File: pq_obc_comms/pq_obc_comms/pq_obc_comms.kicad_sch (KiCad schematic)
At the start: 70 parts, among them J1 Conn_01x10, J2 Conn_01x10, J3 Conn_01x10, J4 Conn_01x10, J6 U.FL, U1 STM32L476RGTx, U2 SX1262IMLTRT, U3 BD2232G-GTR, U4 BD2232G-GTR, U5 BGS12PL6E6327XTSA1, U6 BD2232G-GTR, U7 BD2232G-GTR, X1 ECS-120-18-33-JEM-TR3, X2 FA-128_32.0000MF20X-K5, X3 ABS09-32.768KHZ-7-T

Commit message: Functional revision and finishing touches part II
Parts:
- added Annotation1: Silkscreen_Annotation, symbols-nsl:Bike, symbol symbols-nsl:Silkscreen_Annotation
- U5: footprint GGS_RF:PG-TSLP-6-4 -> rf-nsl:PG-TSLP-6-4
- X1: footprint GGS_Miscellaneous:ECX-32 -> miscelaneous-nsl:ECX-32
- X2: footprint GGS_Miscellaneous:EPSON_FA128 -> miscelaneous-nsl:EPSON_FA128
- X3: footprint GGS_Miscellaneous:ABS09 -> miscelaneous-nsl:ABS09
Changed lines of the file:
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@@
     (pin "1")
   )
+  (symbol (lib_id "symbols-nsl:Silkscreen_Annotation") (at 247.65 58.42 0) (unit 1)
+    (in_bom yes) (on_board yes) (fields_autoplaced)
+    (property "Reference" "Annotation1" (id 0) (at 254 51.4349 0)
+      (effects (font (size 1.27 1.27)) (justify left))
+    )
+    (property "Value" "Silkscreen_Annotation" (id 1) (at 254 53.9749 0)
+      (effects (font (size 1.27 1.27)) (justify left))
+    )
+    (property "Footprint" "symbols-nsl:Bike" (id 2) (at 247.65 58.42 0)
+      (effects (font (size 1.27 1.27)) hide)
+    )
+    (property "Datasheet" "" (id 3) (at 247.65 58.42 0)
+      (effects (font (size 1.27 1.27)) hide)
+    )
+  )
   (symbol (lib_id "power:GND") (at 116.84 25.4 0) (unit 1)
     (in_bom yes) (on_board yes)
@@
     (property "Reference" "U5" (id 0) (at 184.15 22.86 0))
     (property "Value" "BGS12PL6E6327XTSA1" (id 1) (at 184.15 25.4 0))
-    (property "Footprint" "GGS_RF:PG-TSLP-6-4" (id 2) (at 184.15 33.02 0)
+    (property "Footprint" "rf-nsl:PG-TSLP-6-4" (id 2) (at 184.15 33.02 0)
       (effects (font (size 1.27 1.27)) hide)
     )
@@
       (effects (font (size 1.27 1.27)) (justify left))
     )
-    (property "Footprint" "GGS_Miscellaneous:EPSON_FA128" (id 2) (at 259.08 29.21 0)
+    (property "Footprint" "miscelaneous-nsl:EPSON_FA128" (id 2) (at 259.08 29.21 0)
       (effects (font (size 1.27 1.27)) hide)
     )
@@
     (property "Reference" "X3" (id 0) (at 219.71 142.24 0))
     (property "Value" "ABS09-32.768KHZ-7-T" (id 1) (at 219.71 144.78 0))
-    (property "Footprint" "GGS_Miscellaneous:ABS09" (id 2) (at 219.71 148.59 0)
+    (property "Footprint" "miscelaneous-nsl:ABS09" (id 2) (at 219.71 148.59 0)
       (effects (font (size 1.27 1.27)) hide)
     )
@@
       (effects (font (size 1.27 1.27)) (justify left))
     )
-    (property "Footprint" "GGS_Miscellaneous:ECX-32" (id 2) (at 260.35 151.13 0)
+    (property "Footprint" "miscelaneous-nsl:ECX-32" (id 2) (at 260.35 151.13 0)
       (effects (font (size 1.27 1.27)) hide)
     )
@@
       (reference "#PWR0149") (unit 1) (value "GND") (footprint "")
     )
+    (path "/0e0a9cdf-3063-4090-b911-679c5a730d38"
+      (reference "Annotation1") (unit 1) (value "Silkscreen_Annotation") (footprint "symbols-nsl:Bike")
+    )
     (path "/70f6326e-6380-4875-aac5-5e40eda2ece8"
       (reference "C1") (unit 1) (value "47nF") (footprint "Capacitor_SMD:C_0402_1005Metric")
@@
     )
     (path "/1e73ef1c-3a42-4d69-9bb9-affa28519ebc"
-      (reference "U5") (unit 1) (value "BGS12PL6E6327XTSA1") (footprint "GGS_RF:PG-TSLP-6-4")
+      (reference "U5") (unit 1) (value "BGS12PL6E6327XTSA1") (footprint "rf-nsl:PG-TSLP-6-4")
     )
     (path "/5b2c5bc3-5fa8-4d93-ab7a-d6c8c3adc44e"
@@
     )
     (path "/aee54727-eead-440f-9fa9-5ccf5d66a20e"
-      (reference "X1") (unit 1) (value "ECS-120-18-33-JEM-TR3") (footprint "GGS_Miscellaneous:ECX-32")
+      (reference "X1") (unit 1) (value "ECS-120-18-33-JEM-TR3") (footprint "miscelaneous-nsl:ECX-32")
     )
     (path "/7ef30fbc-71e7-4186-a1d8-48087b5069c5"
-      (reference "X2") (unit 1) (value "FA-128_32.0000MF20X-K5") (footprint "GGS_Miscellaneous:EPSON_FA128")
+      (reference "X2") (unit 1) (value "FA-128_32.0000MF20X-K5") (footprint "miscelaneous-nsl:EPSON_FA128")
     )
     (path "/89691019-6129-4efd-9407-b4187a9c6ccc"
-      (reference "X3") (unit 1) (value "ABS09-32.768KHZ-7-T") (footprint "GGS_Miscellaneous:ABS09")
+      (reference "X3") (unit 1) (value "ABS09-32.768KHZ-7-T") (footprint "miscelaneous-nsl:ABS09")
     )
   )

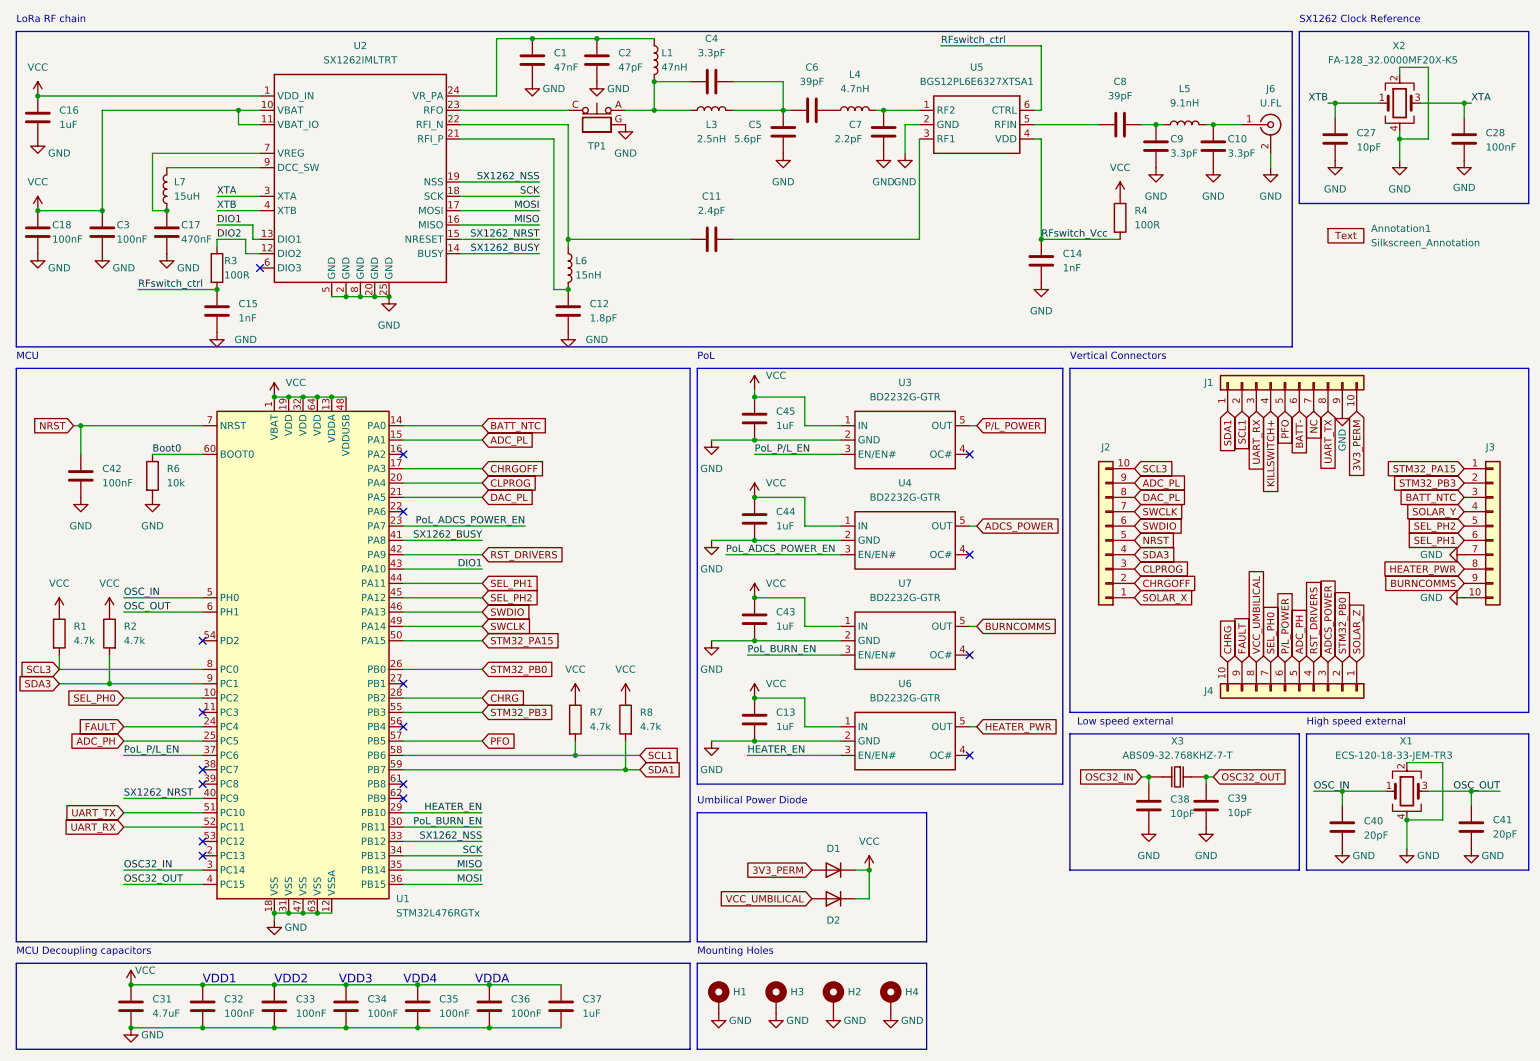
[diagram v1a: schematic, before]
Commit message: Full Kicad7 transition, library improvement and adaptation, correct footprints and 3D models added
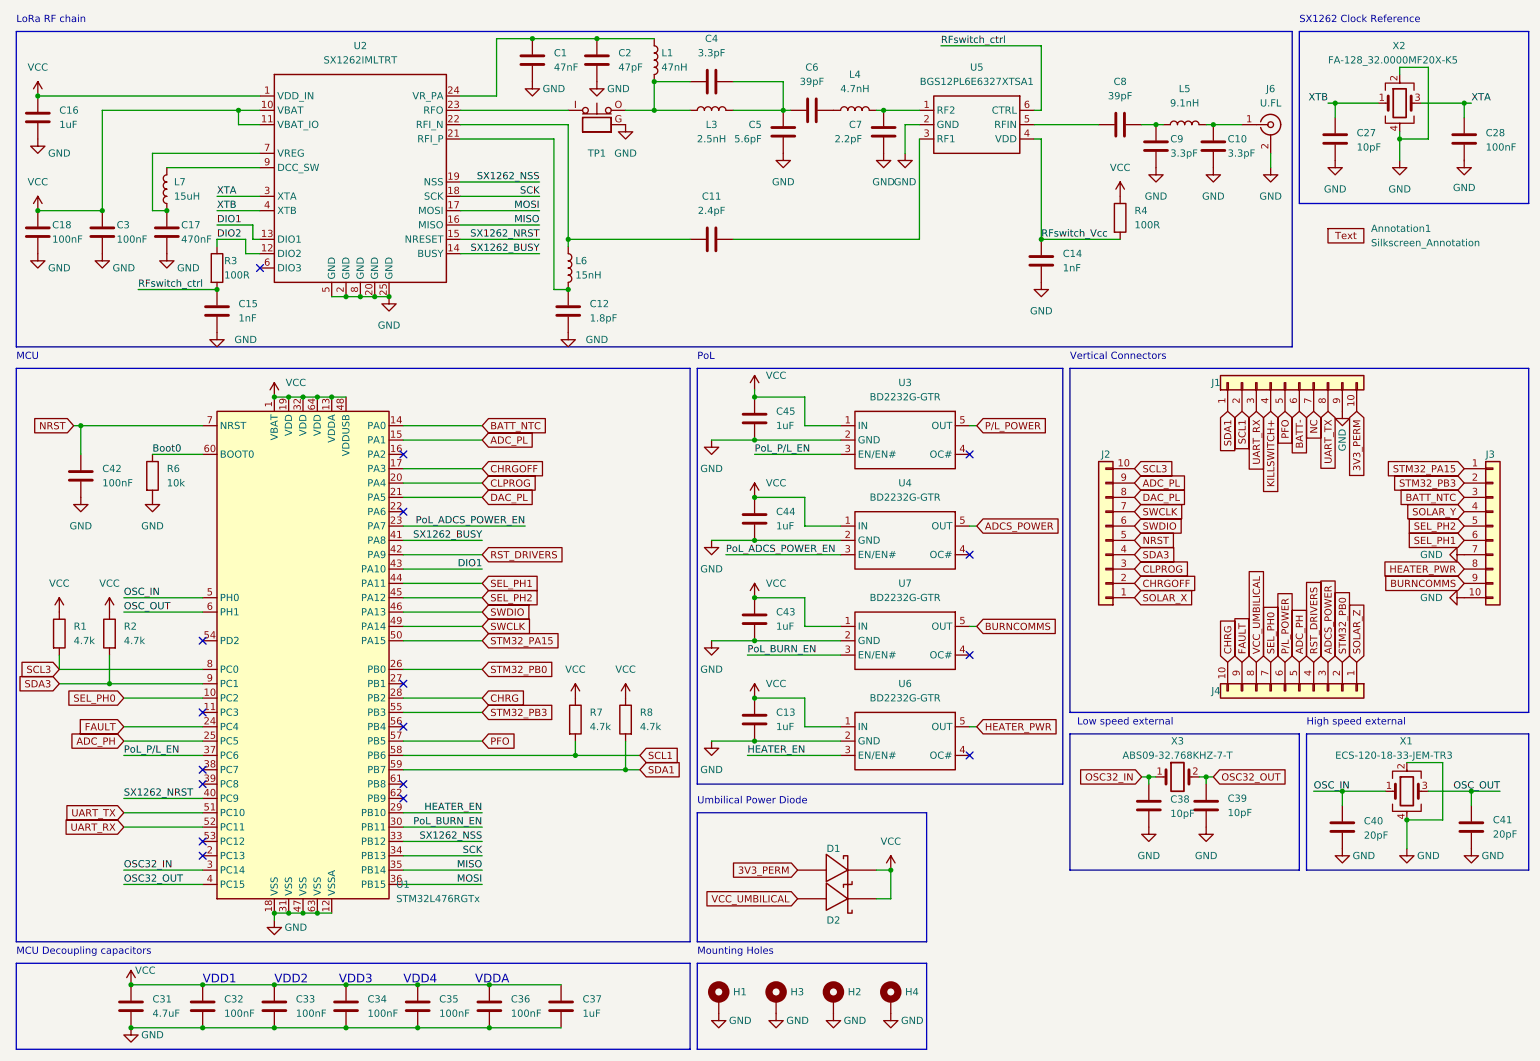
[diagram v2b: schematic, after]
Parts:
- Annotation1: footprint symbols-nsl:Bike -> -nsl_symbols:Bike; symbol symbols-nsl:Silkscreen_Annotation -> -nsl_symbols:Silkscreen_Annotation
- D1, D2: value RBS1LAM40ATR -> ${SIM.PARAMS}; footprint Diode_SMD:D_SOD-128 -> -nsl_passive:RBS1LAM40ATR_Schottky; symbol Simulation_SPICE:DIODE -> -nsl_passive:RBS1LAM40ATR_Schottky; Spice_Netlist_Enabled Y -> (none); Spice_Primitive D -> (none)
- J1, J2, J3, J4: footprint Connector_PinSocket_2.54mm:PinSocket_1x10_P2.54mm_Vertical -> -nsl_connector:SLW-110-01; symbol Connector_Generic:Conn_01x10 -> -nsl_connector:SLW-110-01
- TP1: footprint Connector_Coaxial:CoaxialSwitch_Hirose_MS-156C3_Horizontal -> -nsl_connector:CoaxialSwitch_Hirose_MS-156C3_Horizontal; symbol Connector:CoaxialSwitch_Testpoint -> -nsl_connector:MS-156C
- U1: symbol MCU_ST_STM32L4:STM32L476RGTx -> -nsl_mcu:STM32L476RGT
- U2: symbol COMMS-altium-import:0_SX1262IMLTRT -> -nsl_rf:SX1262IML
- U3, U4, U6, U7: symbol COMMS-altium-import:0_BD2232G-GTR -> -nsl_power:BD2232G
- U5: footprint rf-nsl:PG-TSLP-6-4 -> -nsl_rf:PG-TSLP-6-4; symbol COMMS-altium-import:0_RFswitch -> -nsl_rf:BGS12PL6E632
- X1: footprint miscelaneous-nsl:ECX-32 -> -nsl_miscellaneous:ECX-32
- X2: footprint miscelaneous-nsl:EPSON_FA128 -> -nsl_miscellaneous:EPSON_FA128
- X3: footprint miscelaneous-nsl:ABS09 -> -nsl_miscellaneous:ABS09; symbol COMMS-altium-import:0_32.768KHz -> -nsl_miscellaneous:ABS09
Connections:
- net 3V3_PERM: now also D1.2; no longer D1.1 (A)
- net VCC: now also D1.1, D2.1; no longer D1.2 (K), D2.2 (K)
- net VCC_UMBILICAL: now also D2.2; no longer D2.1 (A)
- net at U2.23 (RFO): now also TP1.I; no longer TP1.C
- net at C4.1, L1.2, L3.1: now also TP1.O; no longer TP1.A

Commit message: Added adaptive resistive network for battery chemistry and charge voltage flexibility & connected all the PoLs + COMMS to 3V3_perm instead of VCC (3.3V - schottky diode)
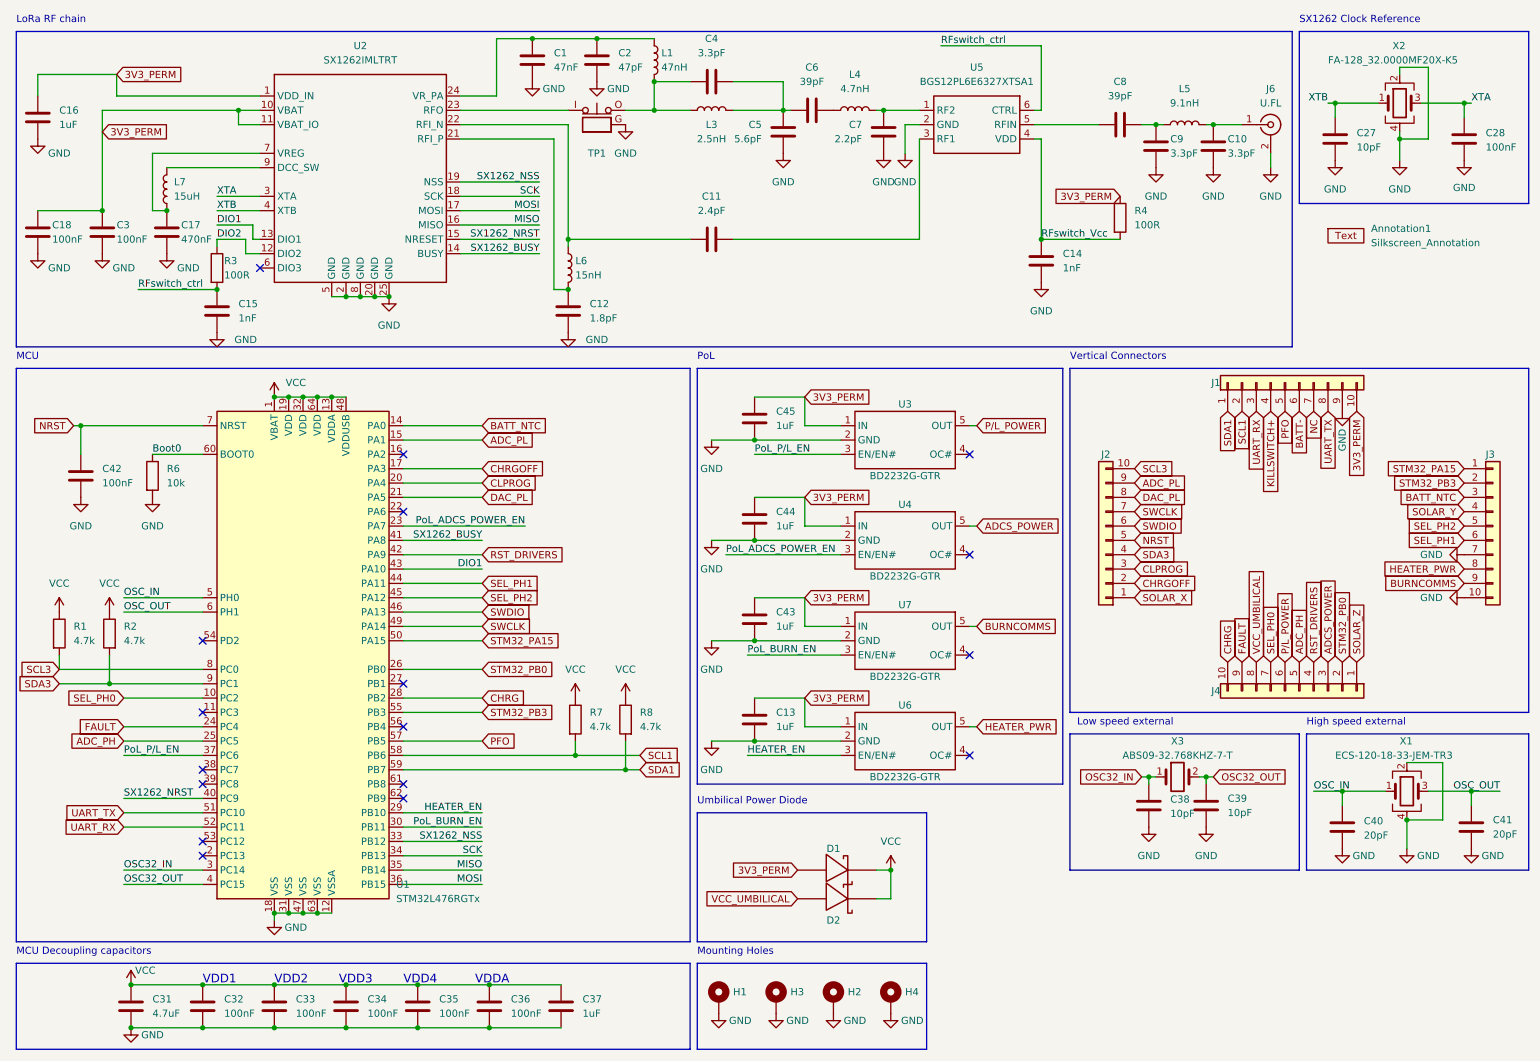
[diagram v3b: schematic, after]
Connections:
- net 3V3_PERM: now also C13.1, C16.1, C18.1, C3.1, C43.1, C44.1, C45.2, R4.1, U2.1 (VDD_IN), U2.10 (VBAT), U2.11 (VBAT_IO), U3.1 (IN), U4.1 (IN), U6.1 (IN), U7.1 (IN)
- net VCC: no longer C13.1, C16.1, C18.1, C3.1, C43.1, C44.1, C45.2, R4.1, U2.1 (VDD_IN), U2.10 (VBAT), U2.11 (VBAT_IO), U3.1 (IN), U4.1 (IN), U6.1 (IN), U7.1 (IN)

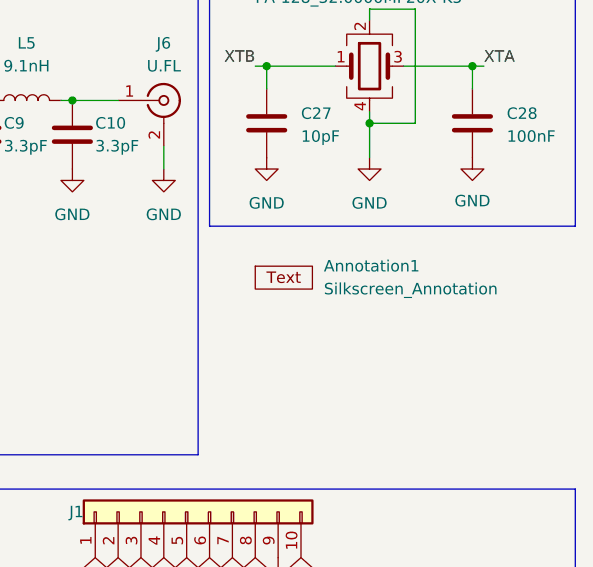
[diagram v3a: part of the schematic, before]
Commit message: PoL & SX1262 feeding at 3.3V and OBC feeding at 3.1 (Schottky diode) strategy changed from inner layer 2 plane to 1 mm thick traces
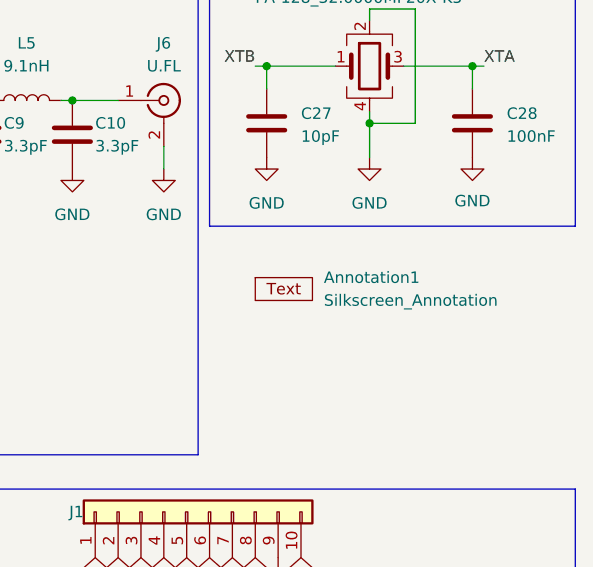
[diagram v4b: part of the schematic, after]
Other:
- moved on the sheet: Annotation1
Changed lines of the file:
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@@
     )
   )
-  (symbol (lib_id "-nsl_symbols:Silkscreen_Annotation") (at 247.65 58.42 0) (unit 1)
+  (symbol (lib_id "-nsl_symbols:Silkscreen_Annotation") (at 247.65 59.69 0) (unit 1)
     (in_bom yes) (on_board yes) (dnp no) (fields_autoplaced)
-    (property "Reference" "Annotation1" (at 254 51.4349 0)
+    (property "Reference" "Annotation1" (at 254 52.7049 0)
       (effects (font (size 1.27 1.27)) (justify left))
     )
-    (property "Value" "Silkscreen_Annotation" (at 254 53.9749 0)
+    (property "Value" "Silkscreen_Annotation" (at 254 55.2449 0)
       (effects (font (size 1.27 1.27)) (justify left))
     )
-    (property "Footprint" "-nsl_symbols:Bike" (at 247.65 58.42 0)
+    (property "Footprint" "-nsl_symbols:Bike" (at 247.65 59.69 0)
       (effects (font (size 1.27 1.27)) hide)
     )
-    (property "Datasheet" "" (at 247.65 58.42 0)
+    (property "Datasheet" "" (at 247.65 59.69 0)
       (effects (font (size 1.27 1.27)) hide)
     )

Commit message: fix the mirror on the external crystal of the OBC
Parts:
- X1: footprint -nsl_miscellaneous:ECX-32 -> miscelaneous-nsl:ECX-32
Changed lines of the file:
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@@
       (effects (font (size 1.27 1.27)) (justify left))
     )
-    (property "Footprint" "-nsl_miscellaneous:ECX-32" (at 260.35 151.13 0)
+    (property "Footprint" "miscelaneous-nsl:ECX-32" (at 260.35 151.13 0)
       (effects (font (size 1.27 1.27)) hide)
     )
